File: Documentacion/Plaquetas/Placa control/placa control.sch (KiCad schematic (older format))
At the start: 45 parts, among them J1 Conn_01x02_Male, J10 Conn_01x06_Female, J11 Conn_01x03_Male, J12 Conn_01x03_Male, J13 Conn_01x03_Male, J2 DB9_Female_MountingHoles, J3 Screw_Terminal_01x02, J4 Conn_01x06_Male, J5 Conn_01x02_Male, J6 Conn_01x04_Male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

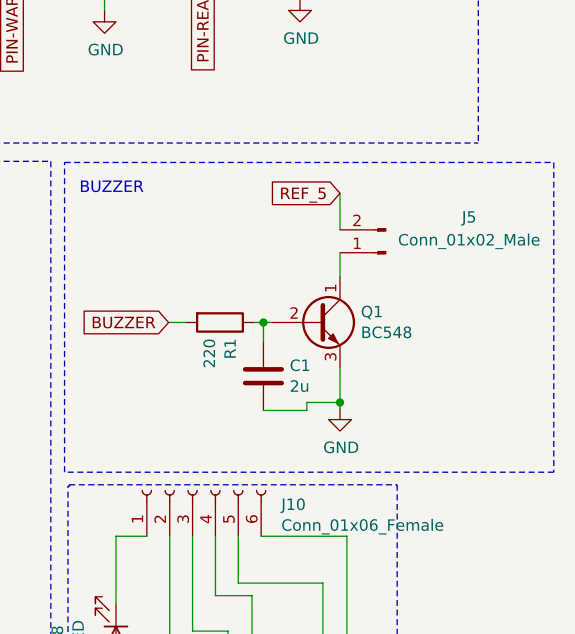
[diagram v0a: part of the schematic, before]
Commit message: changed buzzer to common collector mode
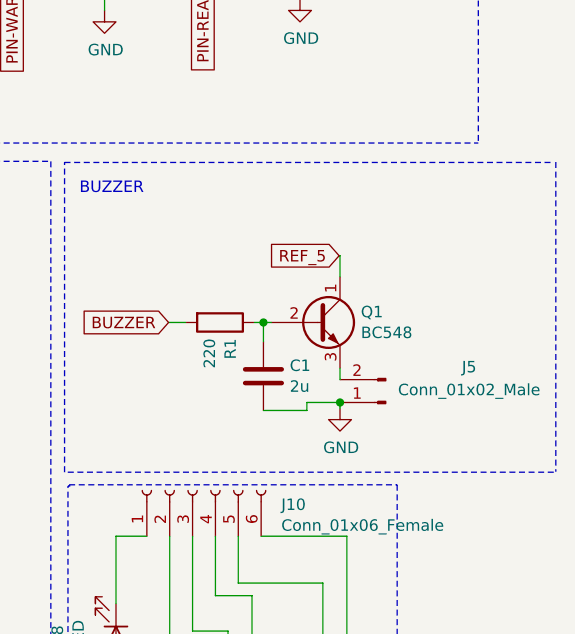
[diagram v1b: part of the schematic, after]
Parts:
- C1, C10, C11, C2, C3, C4, C6, C9: footprint Capacitor_THT:C_Disc_D4.7mm_W2.5mm_P5.00mm -> custom_footprints:C_Disc_D4.7mm_W2.5mm_P5.00mm
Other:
- moved on the sheet: J5
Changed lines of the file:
@@
 F 0 "C9" H 5815 1296 50  0000 L CNN
 F 1 "100n" H 5815 1205 50  0000 L CNN
-F 2 "Capacitor_THT:C_Disc_D4.7mm_W2.5mm_P5.00mm" H 5738 1100 50  0001 C CNN
+F 2 "custom_footprints:C_Disc_D4.7mm_W2.5mm_P5.00mm" H 5738 1100 50  0001 C CNN
 F 3 "~" H 5700 1250 50  0001 C CNN
 	1    5700 1250
@@
 F 0 "C10" H 5990 4771 50  0000 L CNN
 F 1 "4.7n" H 5990 4680 50  0000 L CNN
-F 2 "Capacitor_THT:C_Disc_D4.7mm_W2.5mm_P5.00mm" H 5913 4575 50  0001 C CNN
+F 2 "custom_footprints:C_Disc_D4.7mm_W2.5mm_P5.00mm" H 5913 4575 50  0001 C CNN
 F 3 "~" H 5875 4725 50  0001 C CNN
 	1    5875 4725
@@
 F 0 "C11" H 8025 4586 50  0000 L CNN
 F 1 "4.7n" H 8025 4495 50  0000 L CNN
-F 2 "Capacitor_THT:C_Disc_D4.7mm_W2.5mm_P5.00mm" H 7948 4390 50  0001 C CNN
+F 2 "custom_footprints:C_Disc_D4.7mm_W2.5mm_P5.00mm" H 7948 4390 50  0001 C CNN
 F 3 "~" H 7910 4540 50  0001 C CNN
 	1    7910 4540
@@
 F 0 "C2" H 1115 3881 50  0000 L CNN
 F 1 "100n" H 1115 3790 50  0000 L CNN
-F 2 "Capacitor_THT:C_Disc_D4.7mm_W2.5mm_P5.00mm" H 1038 3685 50  0001 C CNN
+F 2 "custom_footprints:C_Disc_D4.7mm_W2.5mm_P5.00mm" H 1038 3685 50  0001 C CNN
 F 3 "~" H 1000 3835 50  0001 C CNN
 	1    1000 3835
@@
 F 0 "C3" H 1955 3881 50  0000 L CNN
 F 1 "330n" H 1955 3790 50  0000 L CNN
-F 2 "Capacitor_THT:C_Disc_D4.7mm_W2.5mm_P5.00mm" H 1878 3685 50  0001 C CNN
+F 2 "custom_footprints:C_Disc_D4.7mm_W2.5mm_P5.00mm" H 1878 3685 50  0001 C CNN
 F 3 "~" H 1840 3835 50  0001 C CNN
 	1    1840 3835
@@
 F 0 "C4" H 5180 4396 50  0000 L CNN
 F 1 "2.2n" H 5180 4305 50  0000 L CNN
-F 2 "Capacitor_THT:C_Disc_D4.7mm_W2.5mm_P5.00mm" H 5103 4200 50  0001 C CNN
+F 2 "custom_footprints:C_Disc_D4.7mm_W2.5mm_P5.00mm" H 5103 4200 50  0001 C CNN
 F 3 "~" H 5065 4350 50  0001 C CNN
 	1    5065 4350
@@
 F 0 "C6" H 4120 4406 50  0000 L CNN
 F 1 "2.2n" H 4120 4315 50  0000 L CNN
-F 2 "Capacitor_THT:C_Disc_D4.7mm_W2.5mm_P5.00mm" H 4043 4210 50  0001 C CNN
+F 2 "custom_footprints:C_Disc_D4.7mm_W2.5mm_P5.00mm" H 4043 4210 50  0001 C CNN
 F 3 "~" H 4005 4360 50  0001 C CNN
 	1    4005 4360
@@
 L Connector:Conn_01x02_Male J5
 U 1 1 5EBD2A40
-P 10630 3555
-F 0 "J5" H 10265 3400 50  0000 C CNN
-F 1 "Conn_01x02_Male" H 10265 3500 50  0000 C CNN
-F 2 "custom_footprints:PinHeader_1x02_P2.54mm_Vertical" H 10630 3555 50  0001 C CNN
-F 3 "~" H 10630 3555 50  0001 C CNN
-	1    10630 3555
+P 10630 4210
+F 0 "J5" H 10265 4055 50  0000 C CNN
+F 1 "Conn_01x02_Male" H 10265 4155 50  0000 C CNN
+F 2 "custom_footprints:PinHeader_1x02_P2.54mm_Vertical" H 10630 4210 50  0001 C CNN
+F 3 "~" H 10630 4210 50  0001 C CNN
+	1    10630 4210
 	-1   0    0    1
 $EndComp
-Wire Wire Line
-	10430 3660 10430 3555
 Wire Wire Line
 	10430 4235 10430 4210
@@
 Text Notes 9290 3305 0    50   ~ 0
 BUZZER\n
-Wire Wire Line
-	10430 3455 10430 3295
-Text GLabel 10430 3295 0    50   Input ~ 0
+Text GLabel 10426 3568 0    50   Input ~ 0
 REF_5
 Wire Notes Line
 	9225 3160 11365 3160
-Wire Notes Line
-	11365 3160 11365 4515
 Wire Notes Line
 	11365 4515 9225 4515
@@
 F 0 "C1" H 10210 4141 50  0000 L CNN
 F 1 "2u" H 10210 4050 50  0000 L CNN
-F 2 "Capacitor_THT:C_Disc_D4.7mm_W2.5mm_P5.00mm" H 10133 3945 50  0001 C CNN
+F 2 "custom_footprints:C_Disc_D4.7mm_W2.5mm_P5.00mm" H 10133 3945 50  0001 C CNN
 F 3 "~" H 10095 4095 50  0001 C CNN
 	1    10095 4095
@@
 Wire Wire Line
 	10285 4210 10430 4210
-Connection ~ 10430 4210
-Wire Wire Line
-	10430 4210 10430 4060
 Wire Wire Line
 	10095 3860 10095 3945
@@
 $EndComp
 NoConn ~ 4100 1330
+Wire Notes Line
+	11374 3158 11374 4513
+Connection ~ 10430 4210
+Wire Wire Line
+	10430 4060 10430 4110
+Wire Wire Line
+	10430 3660 10430 3568
+Wire Wire Line
+	10430 3568 10426 3568
 $EndSCHEMATC
